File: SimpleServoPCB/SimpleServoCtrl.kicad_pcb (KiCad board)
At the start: 2 copper layers, 94 x 66 mm, 50 parts, among them P1A1 CONN_8, P1B1 CONN_8, P1C1 CONN_8, P2A1 CONN_8, P2B1 CONN_8, P2C1 CONN_8, P3 Prog, P4 I2C, P5 Power, SW1 SW_PUSH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

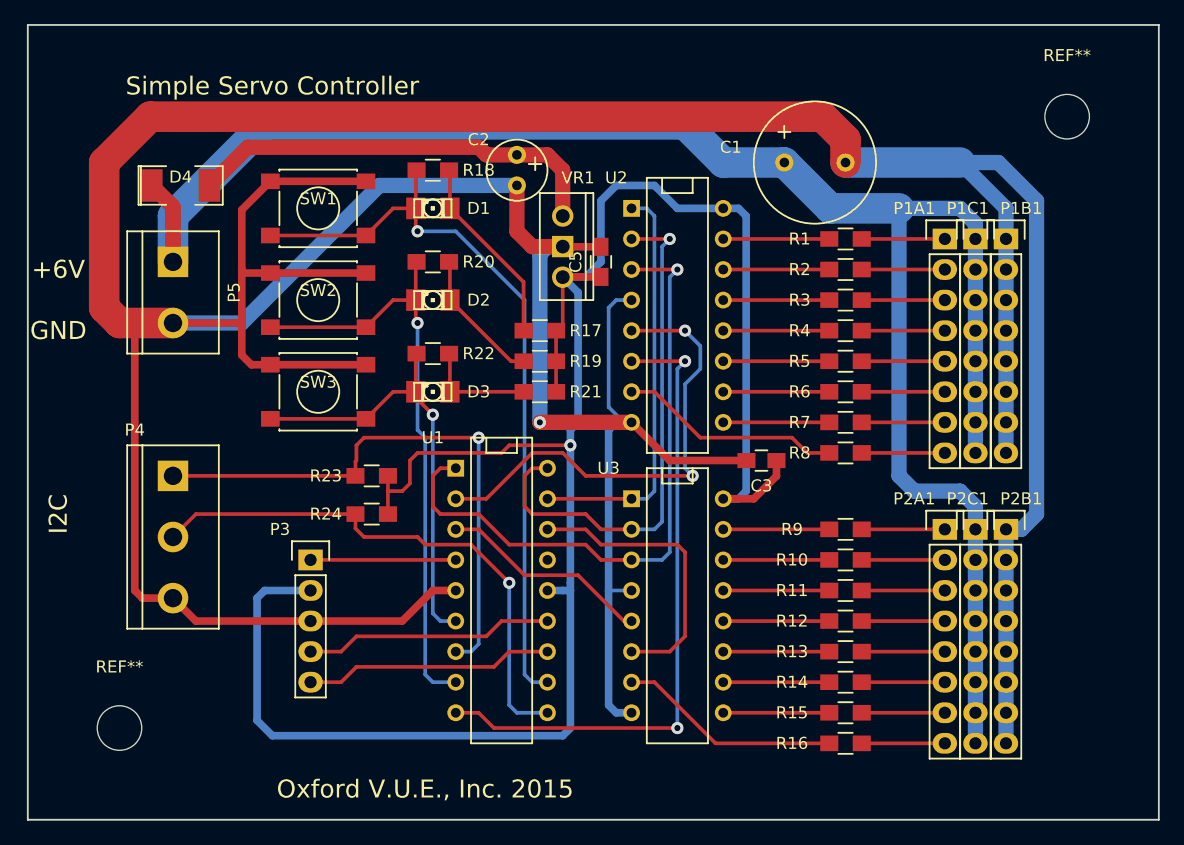
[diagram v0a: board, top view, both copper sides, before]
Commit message: Added Packet Serial version
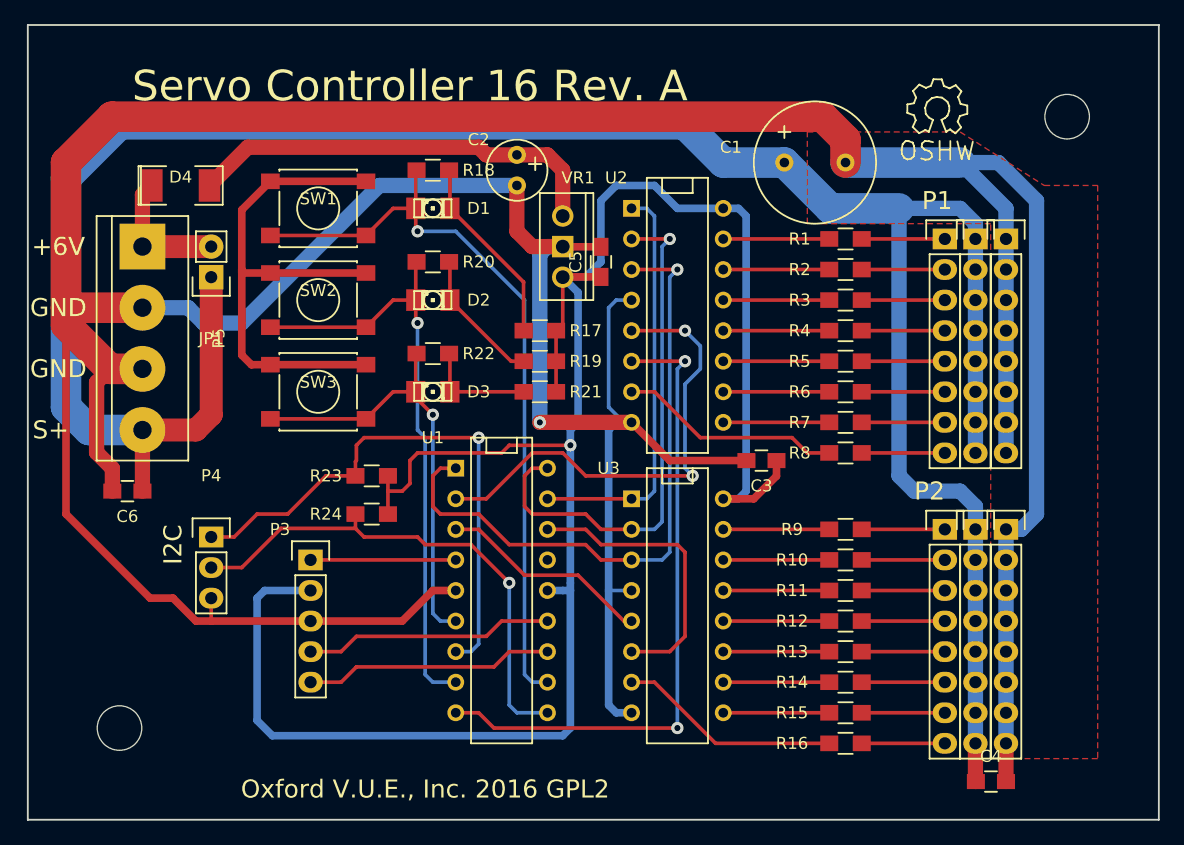
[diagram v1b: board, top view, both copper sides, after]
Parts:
- added C4: 0.1uF, Capacitors_SMD:C_0805_HandSoldering, F.Cu at (186.7, 151.8)
- added C6: 0.1uF, Capacitors_SMD:C_0805_HandSoldering, F.Cu at (115.0, 127.6)
- added JP1: Jumper_NO_Small, Pin_Headers:Pin_Header_Straight_1x02, F.Cu at (121.9, 109.9)
- added SIM1: Symbol_OSHW-Logo_SilkScreen, Symbols:Symbol_OSHW-Logo_SilkScreen, F.Cu at (182.2, 95.9)
- P4: footprint Connect:bornier3 -> Pin_Headers:Pin_Header_Straight_1x03
- P5: value Power -> CONN_01X04; footprint Connect:bornier2 -> Connect:bornier4
- R23, R24: value 4.7KΩ -> 47KΩ
- moved P5 4.58 mm to (116.2, 114.9)
- moved P4 3.17 mm to (121.9, 131.4), turned to 0 degrees
- renumbered REF** to H1, REF** to H2
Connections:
- D4 pad 1: +BATT -> Net-(D4-Pad1)
- P5 pad 1: +BATT -> Net-(D4-Pad1)
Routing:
- net +BATT: track 153.8 -> 202.6 mm
- net GND: track 399.3 -> 424.5 mm
- net Net-(D4-Pad1): track 0.00 -> 11.1 mm
- net Net-(P4-Pad2): track 45.4 -> 42.8 mm
- net Net-(P4-Pad1): track 47.5 -> 46.4 mm
- added copper zone on F.Cu, net GND
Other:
- board text added: "Oxford V.U.E., Inc. 2016 GPL2"
- board text added: "P1"
- board text added: "P2"
- board text added: "S+"
- board text added: "Servo Controller 16 Rev. A"
- board text removed: "Oxford V.U.E., Inc. 2015"
- board text removed: "Simple Servo Controller"
